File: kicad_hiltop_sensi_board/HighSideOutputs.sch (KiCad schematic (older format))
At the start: 36 parts, among them Q10 ZXMN6A07F, Q11 ZXMN6A07F, Q7 ZXMN6A07F, Q8 ZXMN6A07F, U14 BTS4140N, U15 BTS4140N, U17 BTS4140N, U18 BTS4140N

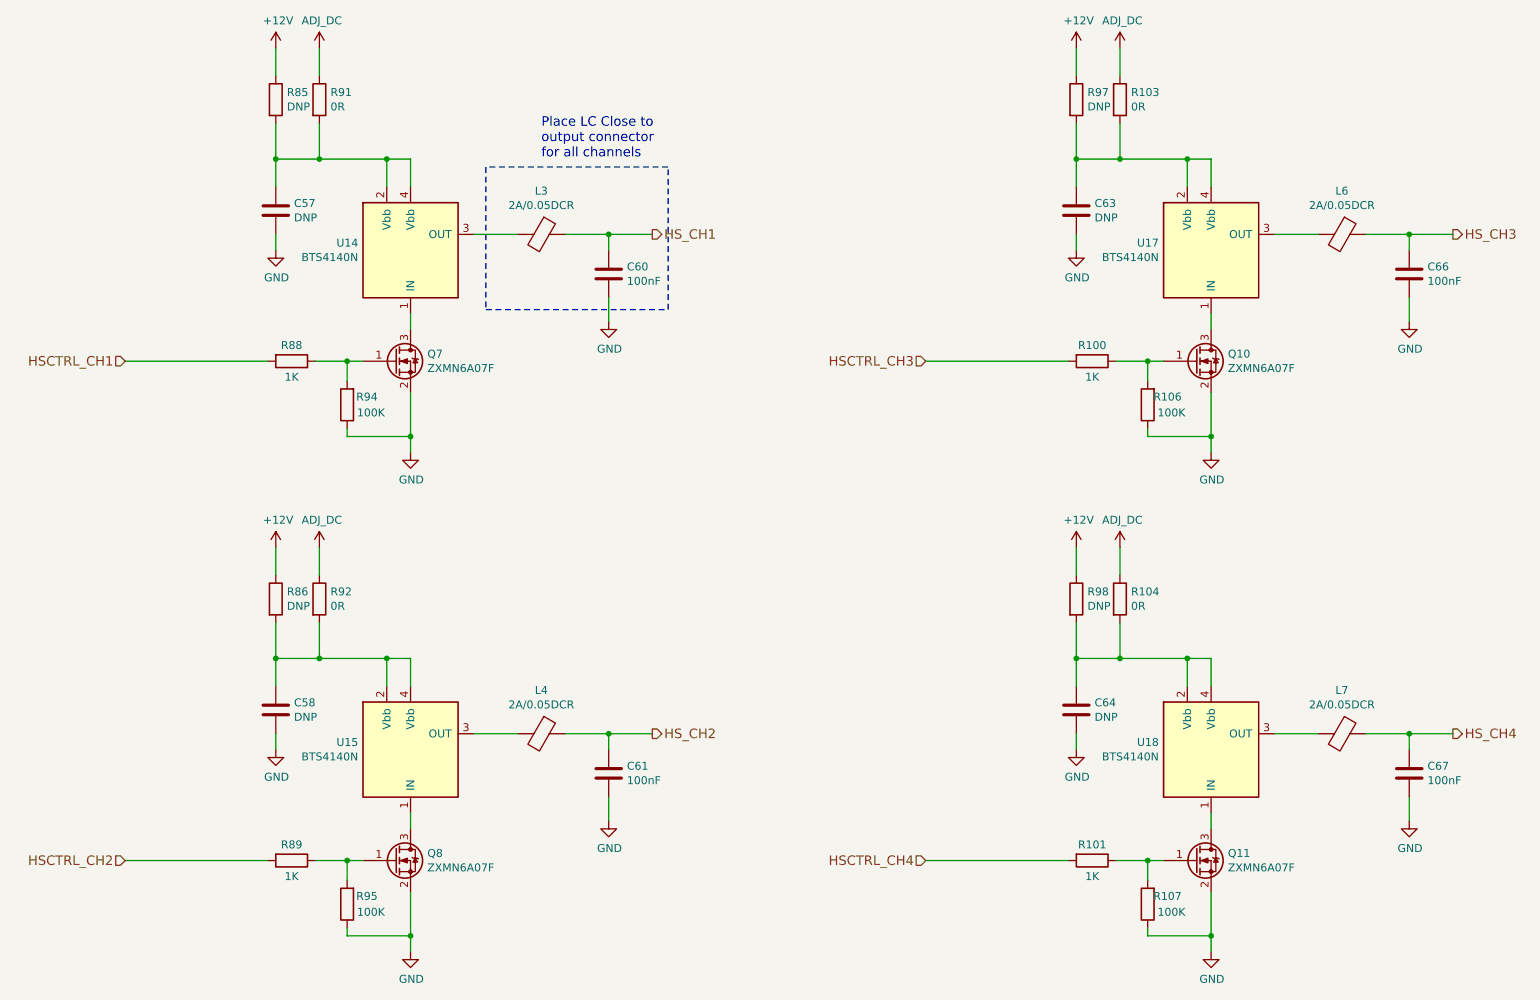
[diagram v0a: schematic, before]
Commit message: Updated sensi board pin map and layout before PCB tracking
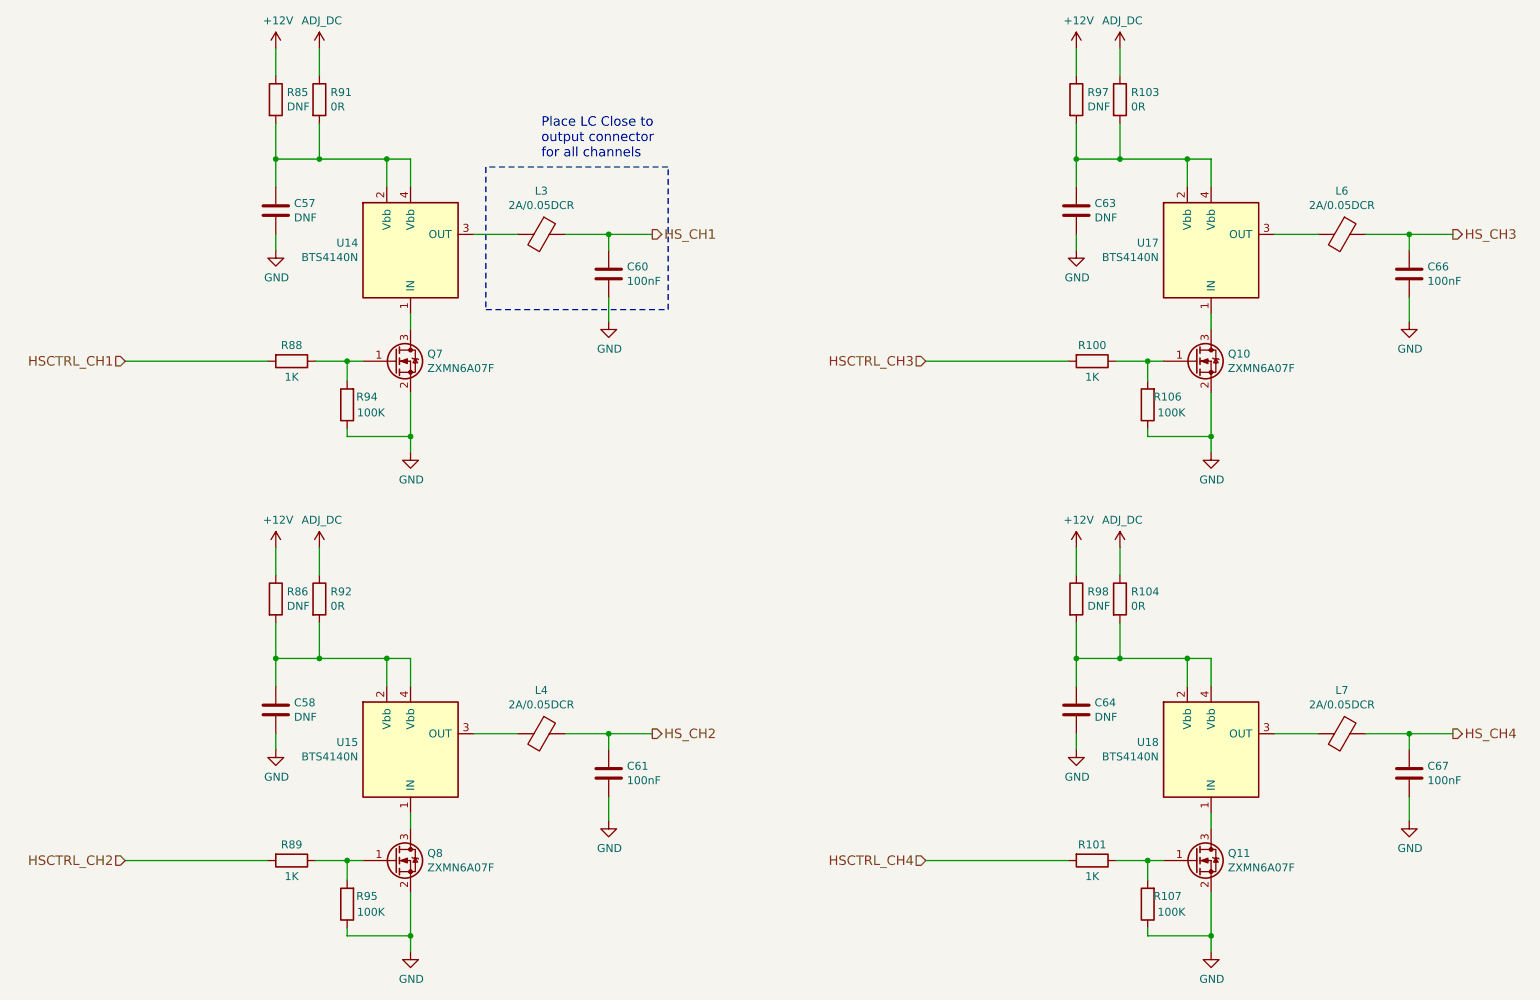
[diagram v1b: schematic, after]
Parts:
- C57, C58, C63, C64: value DNP -> DNF
- R103, R104, R91, R92: Devtank (none) -> 101-006
- R85, R86, R97, R98: value DNP -> DNF; Devtank 101-006 -> (none)
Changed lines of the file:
@@
 P 2675 1750
 F 0 "R85" H 2745 1796 50  0000 L CNN
-F 1 "DNP" H 2745 1705 50  0000 L CNN
+F 1 "DNF" H 2745 1705 50  0000 L CNN
 F 2 "Resistor_SMD:R_0805_2012Metric" V 2605 1750 50  0001 C CNN
 F 3 "" H 2675 1750 50  0001 C CNN
-F 4 "101-006" H 0   0   50  0001 C CNN "Devtank"
+F 4 "" H 0   0   50  0001 C CNN "Devtank"
 	1    2675 1750
 	1    0    0    -1
@@
 F 2 "Resistor_SMD:R_0805_2012Metric" V 2880 1750 50  0001 C CNN
 F 3 "" H 2950 1750 50  0001 C CNN
+F 4 "101-006" H 2950 1750 50  0001 C CNN "Devtank"
 	1    2950 1750
 	1    0    0    -1
@@
 P 2675 2450
 F 0 "C57" H 2790 2496 50  0000 L CNN
-F 1 "DNP" H 2790 2405 50  0000 L CNN
+F 1 "DNF" H 2790 2405 50  0000 L CNN
 F 2 "Capacitor_SMD:C_0805_2012Metric" H 2713 2300 50  0001 C CNN
 F 3 "" H 2675 2450 50  0001 C CNN
@@
 P 2675 4900
 F 0 "R86" H 2745 4946 50  0000 L CNN
-F 1 "DNP" H 2745 4855 50  0000 L CNN
+F 1 "DNF" H 2745 4855 50  0000 L CNN
 F 2 "Resistor_SMD:R_0805_2012Metric" V 2605 4900 50  0001 C CNN
 F 3 "" H 2675 4900 50  0001 C CNN
-F 4 "101-006" H 0   0   50  0001 C CNN "Devtank"
+F 4 "" H 0   0   50  0001 C CNN "Devtank"
 	1    2675 4900
 	1    0    0    -1
@@
 F 2 "Resistor_SMD:R_0805_2012Metric" V 2880 4900 50  0001 C CNN
 F 3 "" H 2950 4900 50  0001 C CNN
+F 4 "101-006" H 2950 4900 50  0001 C CNN "Devtank"
 	1    2950 4900
 	1    0    0    -1
@@
 P 2675 5600
 F 0 "C58" H 2790 5646 50  0000 L CNN
-F 1 "DNP" H 2790 5555 50  0000 L CNN
+F 1 "DNF" H 2790 5555 50  0000 L CNN
 F 2 "Capacitor_SMD:C_0805_2012Metric" H 2713 5450 50  0001 C CNN
 F 3 "" H 2675 5600 50  0001 C CNN
@@
 P 7725 1750
 F 0 "R97" H 7795 1796 50  0000 L CNN
-F 1 "DNP" H 7795 1705 50  0000 L CNN
+F 1 "DNF" H 7795 1705 50  0000 L CNN
 F 2 "Resistor_SMD:R_0805_2012Metric" V 7655 1750 50  0001 C CNN
 F 3 "" H 7725 1750 50  0001 C CNN
-F 4 "101-006" H 0   0   50  0001 C CNN "Devtank"
+F 4 "" H 0   0   50  0001 C CNN "Devtank"
 	1    7725 1750
 	1    0    0    -1
@@
 F 2 "Resistor_SMD:R_0805_2012Metric" V 7930 1750 50  0001 C CNN
 F 3 "" H 8000 1750 50  0001 C CNN
+F 4 "101-006" H 8000 1750 50  0001 C CNN "Devtank"
 	1    8000 1750
 	1    0    0    -1
@@
 P 7725 2450
 F 0 "C63" H 7840 2496 50  0000 L CNN
-F 1 "DNP" H 7840 2405 50  0000 L CNN
+F 1 "DNF" H 7840 2405 50  0000 L CNN
 F 2 "Capacitor_SMD:C_0805_2012Metric" H 7763 2300 50  0001 C CNN
 F 3 "" H 7725 2450 50  0001 C CNN
@@
 P 7725 4900
 F 0 "R98" H 7795 4946 50  0000 L CNN
-F 1 "DNP" H 7795 4855 50  0000 L CNN
+F 1 "DNF" H 7795 4855 50  0000 L CNN
 F 2 "Resistor_SMD:R_0805_2012Metric" V 7655 4900 50  0001 C CNN
 F 3 "" H 7725 4900 50  0001 C CNN
-F 4 "101-006" H 0   0   50  0001 C CNN "Devtank"
+F 4 "" H 0   0   50  0001 C CNN "Devtank"
 	1    7725 4900
 	1    0    0    -1
@@
 F 2 "Resistor_SMD:R_0805_2012Metric" V 7930 4900 50  0001 C CNN
 F 3 "" H 8000 4900 50  0001 C CNN
+F 4 "101-006" H 8000 4900 50  0001 C CNN "Devtank"
 	1    8000 4900
 	1    0    0    -1
@@
 P 7725 5600
 F 0 "C64" H 7840 5646 50  0000 L CNN
-F 1 "DNP" H 7840 5555 50  0000 L CNN
+F 1 "DNF" H 7840 5555 50  0000 L CNN
 F 2 "Capacitor_SMD:C_0805_2012Metric" H 7763 5450 50  0001 C CNN
 F 3 "" H 7725 5600 50  0001 C CNN

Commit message: Most major connections complete and differential tracking done on the Sensi board layout
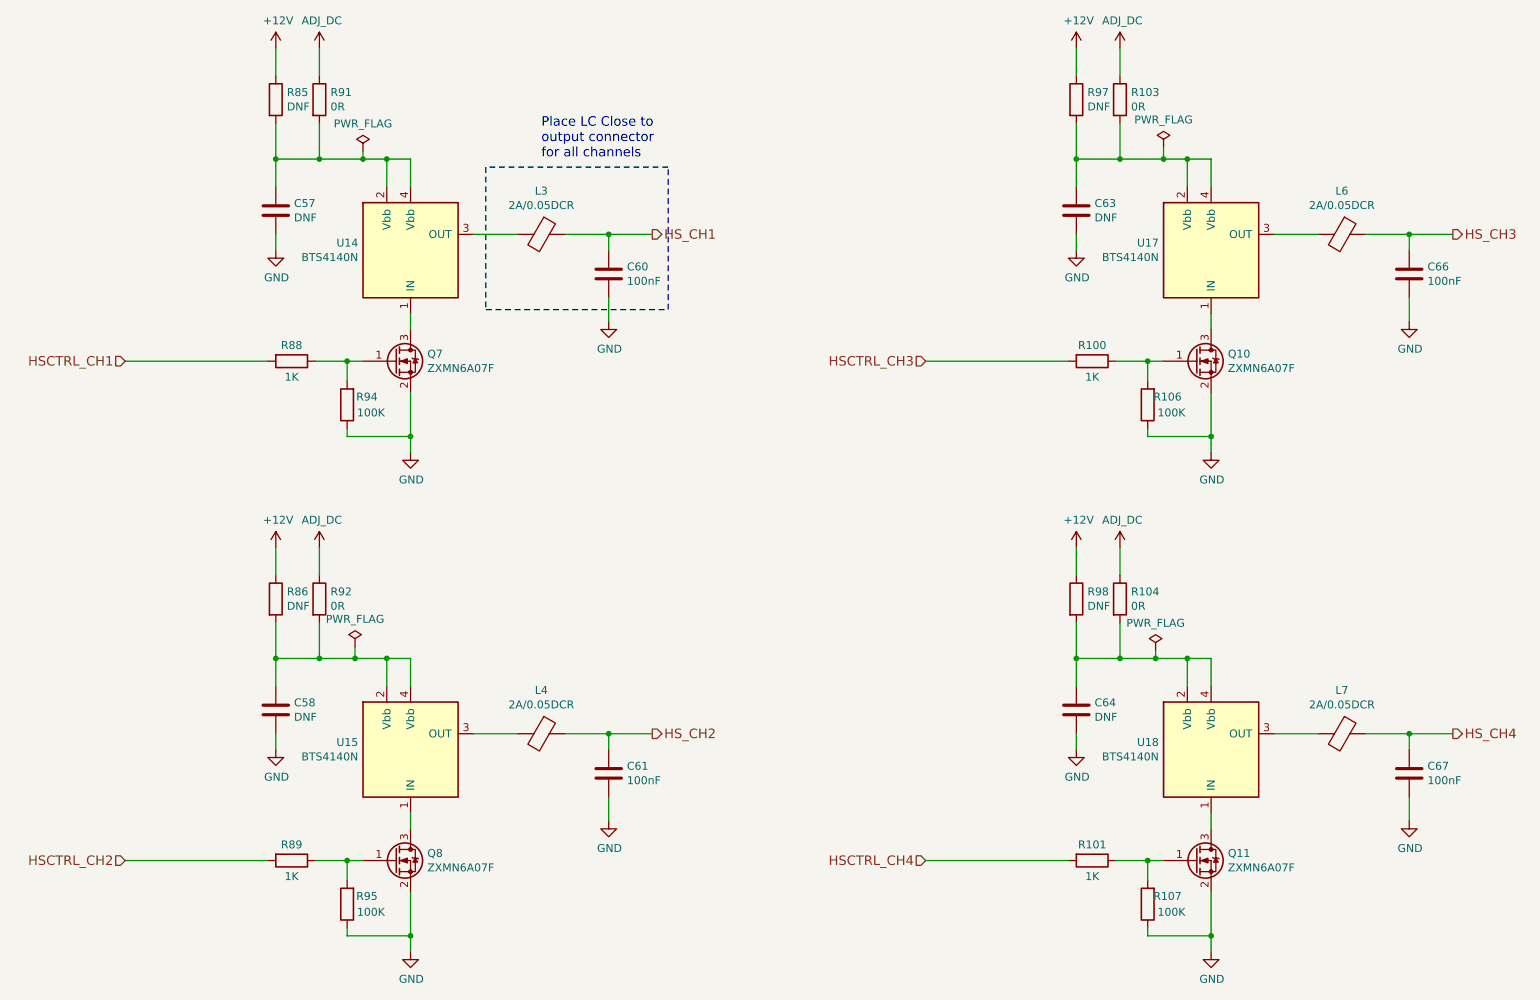
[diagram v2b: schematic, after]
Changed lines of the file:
@@
 $EndComp
 Wire Wire Line
-	2950 2125 3375 2125
+	2950 2125 3225 2125
 Wire Wire Line
 	2675 2125 2950 2125
@@
 $EndComp
 Wire Wire Line
-	2950 5275 3375 5275
+	2950 5275 3175 5275
 Wire Wire Line
 	2675 5275 2950 5275
@@
 $EndComp
 Wire Wire Line
-	8000 2125 8425 2125
+	8000 2125 8275 2125
 Wire Wire Line
 	7725 2125 8000 2125
@@
 $EndComp
 Wire Wire Line
-	8000 5275 8425 5275
+	8000 5275 8225 5275
 Wire Wire Line
 	7725 5275 8000 5275
@@
 Wire Wire Line
 	6775 3400 7675 3400
+$Comp
+L power:PWR_FLAG #FLG0103
+U 1 1 5DAFEB2C
+P 3225 2075
+F 0 "#FLG0103" H 3225 2150 50  0001 C CNN
+F 1 "PWR_FLAG" H 3225 2248 50  0000 C CNN
+F 2 "" H 3225 2075 50  0001 C CNN
+F 3 "" H 3225 2075 50  0001 C CNN
+	1    3225 2075
+	1    0    0    -1
+$EndComp
+$Comp
+L power:PWR_FLAG #FLG0111
+U 1 1 5DB016D3
+P 8275 2050
+F 0 "#FLG0111" H 8275 2125 50  0001 C CNN
+F 1 "PWR_FLAG" H 8275 2223 50  0000 C CNN
+F 2 "" H 8275 2050 50  0001 C CNN
+F 3 "" H 8275 2050 50  0001 C CNN
+	1    8275 2050
+	1    0    0    -1
+$EndComp
+$Comp
+L power:PWR_FLAG #FLG0112
+U 1 1 5DB06407
+P 3175 5200
+F 0 "#FLG0112" H 3175 5275 50  0001 C CNN
+F 1 "PWR_FLAG" H 3175 5373 50  0000 C CNN
+F 2 "" H 3175 5200 50  0001 C CNN
+F 3 "" H 3175 5200 50  0001 C CNN
+	1    3175 5200
+	1    0    0    -1
+$EndComp
+$Comp
+L power:PWR_FLAG #FLG0113
+U 1 1 5DB0A269
+P 8225 5225
+F 0 "#FLG0113" H 8225 5300 50  0001 C CNN
+F 1 "PWR_FLAG" H 8225 5398 50  0000 C CNN
+F 2 "" H 8225 5225 50  0001 C CNN
+F 3 "" H 8225 5225 50  0001 C CNN
+	1    8225 5225
+	1    0    0    -1
+$EndComp
+Wire Wire Line
+	8225 5225 8225 5275
+Connection ~ 8225 5275
+Wire Wire Line
+	8225 5275 8425 5275
+Wire Wire Line
+	8275 2050 8275 2125
+Connection ~ 8275 2125
+Wire Wire Line
+	8275 2125 8425 2125
+Wire Wire Line
+	3225 2075 3225 2125
+Connection ~ 3225 2125
+Wire Wire Line
+	3225 2125 3375 2125
+Wire Wire Line
+	3175 5200 3175 5275
+Connection ~ 3175 5275
+Wire Wire Line
+	3175 5275 3375 5275
 $EndSCHEMATC
